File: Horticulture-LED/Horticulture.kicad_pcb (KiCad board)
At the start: 2 copper layers, 220 x 22 mm, 67 parts, among them J1 Conn_01x04_Male, J3 Conn_01x04_Male, J4 Conn_01x04_Male, SW1 SW-I2C, SW2 Rotary_Encoder_Switch, U1 TLE4309, U2 TLE4309, U3 TLE4309, U4 TLE4309, U6 STM32F030F4Px, U7 SSD1306

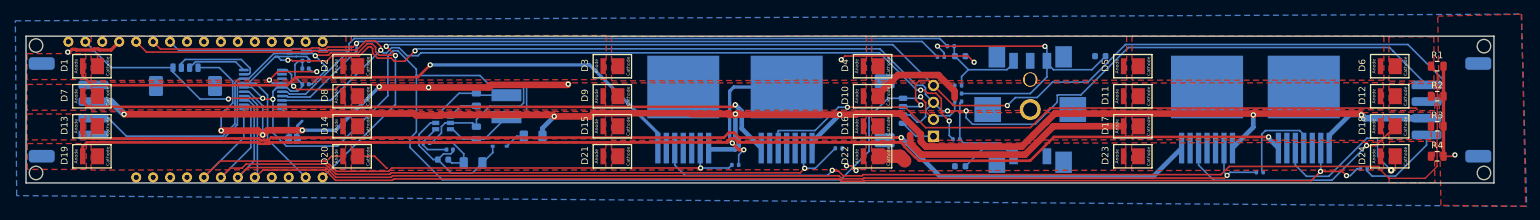
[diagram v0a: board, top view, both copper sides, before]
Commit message: More i2c connectors added, fp for 12c/pwm added, removed stm 32 fp, moved tle drivers
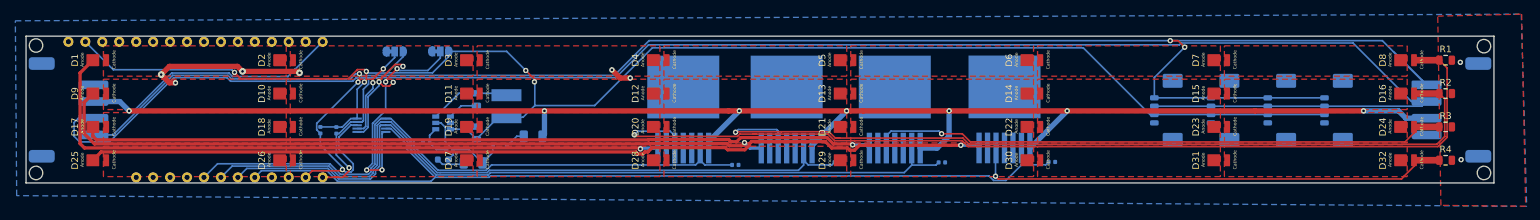
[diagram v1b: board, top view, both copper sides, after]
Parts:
- removed C3, C4, C5: 100nF, Capacitor_SMD:C_0603_1608Metric
- removed J1, Prgrm1: Conn_01x04_Male, Connector_Molex:Molex_PicoBlade_53398-0471_1x04-1MP_P1.25mm_Vertical
- removed R11, R12, R13, R14, R15, R16, R17: 10K2, Resistor_SMD:R_0402_1005Metric
- removed SW1: SW-I2C, Jumper:SolderJumper-2_P1.3mm_Open_RoundedPad1.0x1.5mm
- removed SW2: Rotary_Encoder_Switch, Rotary_Encoder:EC11J1524413-modiied
- removed U6: STM32F030F4Px, Package_SO:TSSOP-20_4.4x6.5mm_P0.65mm
- removed U7: SSD1306, Connector_PinHeader_2.54mm:PinHeader_1x04_P2.54mm_Vertical
- added 3.3v_i2c1: Conn_01x04_Male, Connector_Molex:Molex_PicoBlade_53398-0471_1x04-1MP_P1.25mm_Vertical, B.Cu at (210.3, 91.1)
- added 3.3v_i2c2: Conn_01x04_Male, Connector_Molex:Molex_PicoBlade_53398-0471_1x04-1MP_P1.25mm_Vertical, B.Cu at (218.8, 91.1)
- added 3.3v_i2c3: Conn_01x04_Male, Connector_Molex:Molex_PicoBlade_53398-0471_1x04-1MP_P1.25mm_Vertical, B.Cu at (235.8, 91.1)
- added 3.3v_i2c4: Conn_01x04_Male, Connector_Molex:Molex_PicoBlade_53398-0471_1x04-1MP_P1.25mm_Vertical, B.Cu at (227.3, 91.1)
- added D26: LED, LED_SMD:Sunplus-2835, F.Cu at (78.8, 98.6)
- added D27: LED, LED_SMD:Sunplus-2835, F.Cu at (106.8, 98.6)
- added D28: LED, LED_SMD:Sunplus-2835, F.Cu at (134.8, 98.6)
- added D29: LED, LED_SMD:Sunplus-2835, F.Cu at (162.8, 98.6)
- added D30: LED, LED_SMD:Sunplus-2835, F.Cu at (190.8, 98.6)
- added D31: LED, LED_SMD:Sunplus-2835, F.Cu at (218.8, 98.6)
- added D32: LED, LED_SMD:Sunplus-2835, F.Cu at (246.8, 98.6)
- added D33: D_Schottky, Diode_SMD:D_SOD-323, B.Cu at (111.0, 96.5)
- added JP1: i2c addr 1, Jumper:SolderJumper-3_P1.3mm_Bridged12_RoundedPad1.0x1.5mm_NumberLabels, B.Cu at (102.1, 82.3)
- added JP2: i2c addr 2, Jumper:SolderJumper-3_P1.3mm_Bridged12_RoundedPad1.0x1.5mm_NumberLabels, B.Cu at (95.2, 82.3)
- added U5: PCA9633DP2, Package_TO_SOT_SMD:SOT-552-1-nxp, B.Cu at (91.8, 93.3)
- D1, D10, D11, D12, D13, D14, D15, D16, D17, D18, D19, D2, D20, D21, D22, D23, D24, D3, D4, D5, D7, D8, D9: footprint LED_SMD:Sunplus-35 -> LED_SMD:Sunplus-2835
- D25: value D_Schottky -> LED; footprint Diode_SMD:D_SOD-323 -> LED_SMD:Sunplus-2835; moved to F.Cu
- D6: value LED-purple -> LED; footprint LED_SMD:Sunplus-35 -> LED_SMD:Sunplus-2835
- moved D7 170.3 mm to (218.8, 83.6), turned to 0 degrees
- moved D18 164.3 mm to (78.8, 93.6), turned to 0 degrees
- moved D8 159.3 mm to (246.8, 83.6), turned to 0 degrees
- moved D17 153.8 mm to (50.8, 93.6), turned to 0 degrees
- moved D13 114.4 mm to (162.8, 88.6), turned to 0 degrees
- moved D12 108.3 mm to (134.8, 88.6), turned to 0 degrees
- moved D14 103.4 mm to (190.8, 88.6), turned to 0 degrees
- moved D11 97.8 mm to (106.8, 88.6), turned to 0 degrees
- moved D15 92.4 mm to (218.8, 88.6), turned to 0 degrees
- moved D10 86.8 mm to (78.8, 88.6), turned to 0 degrees
- moved D16 81.4 mm to (246.8, 88.6), turned to 0 degrees
- moved D9 75.8 mm to (50.8, 88.6), turned to 0 degrees
- moved D25 60.3 mm to (50.8, 98.6)
- moved D19 58.4 mm to (106.8, 93.6), turned to 0 degrees
- moved D6 52.3 mm to (190.8, 83.6), turned to 0 degrees
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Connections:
- A1 pad A0: Enc-bt1 -> Net-(A1-PadA0)
- A1 pad A1: Enc-B -> Net-(A1-PadA1)
- A1 pad A2: Enc-A -> Net-(A1-PadA2)
- D13 pad 2: Net-(D13-Pad2) -> Net-(D12-Pad1)
- D17 pad 2: Net-(D16-Pad1) -> Net-(D17-Pad2)
- D19 pad 2: Net-(D19-Pad2) -> Net-(D18-Pad1)
- D25 pad 1: Net-(Cin1-Pad1) -> Net-(D25-Pad1)
- D7 pad 2: Net-(D7-Pad2) -> Net-(D6-Pad1)
- D9 pad 2: Net-(D8-Pad1) -> Net-(D9-Pad2)
- F1 pad 1: Net-(D25-Pad2) -> Net-(D33-Pad2)
- F1 pad 2: VDC -> +24vdc
- J3 pad 3: VDC -> +24vdc
- J4 pad 3: VDC -> +24vdc
- R1 pad 1: Net-(D6-Pad1) -> Net-(D8-Pad1)
- R2 pad 1: Net-(D12-Pad1) -> Net-(D16-Pad1)
- R3 pad 1: Net-(D18-Pad1) -> Net-(D24-Pad1)
- R4 pad 1: Net-(D24-Pad1) -> Net-(D32-Pad1)
- U1 pad 1: VDC -> +24vdc
- U1 pad 5: Net-(D6-Pad1) -> Net-(D8-Pad1)
- U2 pad 1: VDC -> +24vdc
- U2 pad 5: Net-(D12-Pad1) -> Net-(D16-Pad1)
- U2 pad 7: Net-(D7-Pad2) -> Net-(D9-Pad2)
- U3 pad 1: VDC -> +24vdc
- U3 pad 5: Net-(D18-Pad1) -> Net-(D24-Pad1)
- U3 pad 7: Net-(D13-Pad2) -> Net-(D17-Pad2)
- U4 pad 1: VDC -> +24vdc
- U4 pad 5: Net-(D24-Pad1) -> Net-(D32-Pad1)
- U4 pad 7: Net-(D19-Pad2) -> Net-(D25-Pad2)
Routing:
- net Net-(D19-Pad2): track 279.6 -> 0.00 mm, vias 1 -> 0
- net +24vdc: track 0.00 -> 272.4 mm, vias 0 -> 7
- net VDC: track 243.8 -> 0.00 mm, vias 6 -> 0
- net GND: track 256.0 -> 49.6 mm, vias 15 -> 11
- net Net-(D13-Pad2): track 171.6 -> 0.00 mm, vias 1 -> 0
- net Enc-bt1: track 151.8 -> 0.00 mm, vias 3 -> 0
- net Net-(D8-Pad1): track 0.00 -> 148.6 mm, vias 0 -> 1
- net Enc-B: track 136.4 -> 0.00 mm, vias 1 -> 0
- net Net-(D6-Pad1): track 135.7 -> 0.00 mm, vias 1 -> 0
- net Net-(D25-Pad2): track 3.17 -> 135.6 mm, vias 0 -> 1
- net Enc-A: track 132.0 -> 0.00 mm
- net Net-(D17-Pad2): track 0.00 -> 119.1 mm, vias 0 -> 1
- net Net-(D9-Pad2): track 0.00 -> 109.4 mm, vias 0 -> 1
- net Net-(D7-Pad2): track 107.7 -> 0.00 mm, vias 1 -> 0
- net Net-(D12-Pad1): track 102.4 -> 0.00 mm, vias 1 -> 0
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- added copper zone on F.Cu, net Net-(D25-Pad1)
- added copper zone on F.Cu, net Net-(D26-Pad1)
- added copper zone on F.Cu, net Net-(D27-Pad1)
- added copper zone on F.Cu, net Net-(D28-Pad1)
- added copper zone on F.Cu, net Net-(D29-Pad1)
- added copper zone on F.Cu, net Net-(D30-Pad1)
- added copper zone on F.Cu, net Net-(D31-Pad1)
- removed copper zone on F.Cu, net Net-(D1-Pad2)
- removed copper zone on F.Cu, net Net-(D13-Pad2)
- removed copper zone on F.Cu, net Net-(D16-Pad1)
- removed copper zone on F.Cu, net Net-(D19-Pad2)
- removed copper zone on F.Cu, net Net-(D24-Pad1)
- removed copper zone on F.Cu, net Net-(D7-Pad2)
- removed copper zone on F.Cu, net Net-(D8-Pad1)
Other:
- net class Led-Driver: clearance 0.2 -> 0.1; trace_width 0.25 -> 0.8
- net class Led-power: clearance 0.2 -> 0.1; trace_width 0.25 -> 1
- net class VDC: clearance 0.2 -> 0.1; trace_width 1 -> 0.8; via_dia 0.8 -> 1
- net class ymse power: trace_width 0.4 -> 0.5
- board text added: "1.SCL"
- board text added: "2.SDA"
- board text added: "3.+24v"
- board text added: "4.GND"
- board text added: "Horticulture-rev-3.4.0"
- board text removed: "Horticulture-rev-3.3.1"

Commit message: ryddet i resistorer
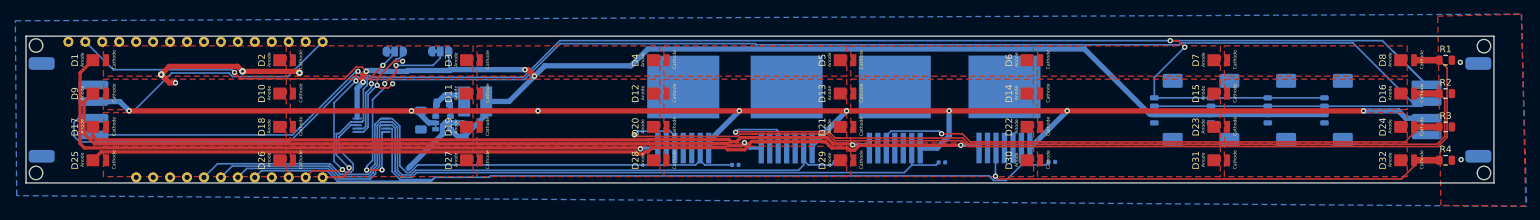
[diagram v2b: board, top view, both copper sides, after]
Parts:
- removed Cinx1: 100nF, Capacitor_SMD:C_0603_1608Metric
- removed D33: D_Schottky, Diode_SMD:D_SOD-323
- removed F1: Polyfuse, Fuse:Fuse_1206_3216Metric
- removed R5, R6: 4.7K, Resistor_SMD:R_0402_1005Metric
- removed Renb1, Rent1: 10k, Resistor_SMD:R_0402_1005Metric
- moved Cin1 10.1 mm to (99.2, 92.6), turned to 270 degrees
- moved Cboot1 5.04 mm to (102.5, 90.0), turned to 0 degrees
- moved L1 4.74 mm to (107.3, 89.8), turned to 270 degrees
- moved Cout1 1.88 mm to (105.7, 94.1)
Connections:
- A1 pad A0: Net-(A1-PadA0) -> (no net)
- A1 pad A1: Net-(A1-PadA1) -> (no net)
- A1 pad A2: Net-(A1-PadA2) -> (no net)
- A1 pad A3: Net-(A1-PadA3) -> (no net)
- A1 pad A4: Net-(A1-PadA4) -> (no net)
- A1 pad A5: Net-(A1-PadA5) -> (no net)
- A1 pad D2: Net-(A1-PadD2) -> (no net)
- A1 pad D3: Net-(A1-PadD3) -> (no net)
- A1 pad D8: Net-(A1-PadD8) -> (no net)
- A1 pad EN: Net-(A1-PadEN) -> (no net)
- A1 pad LI+: Net-(A1-PadLI+) -> (no net)
- A1 pad MD: Net-(A1-PadMD) -> (no net)
- A1 pad MI: Net-(A1-PadMI) -> (no net)
- A1 pad MO: Net-(A1-PadMO) -> (no net)
- A1 pad RESET: Net-(A1-PadRESET) -> (no net)
- A1 pad RX: Net-(A1-PadRX) -> (no net)
- A1 pad SCK: Net-(A1-PadSCK) -> (no net)
- A1 pad TX: Net-(A1-PadTX) -> (no net)
- A1 pad VUSB: Net-(A1-PadVUSB) -> (no net)
- Cin1 pad 1: Net-(Cin1-Pad1) -> +24vdc
- VR1 pad 4: Net-(Renb1-Pad1) -> +24vdc
- VR1 pad 5: Net-(Cin1-Pad1) -> +24vdc
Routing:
- net Net-(Cin1-Pad1): track 15.7 -> 0.00 mm
- net +3.3V: track 238.5 -> 253.8 mm
- net Net-(Renb1-Pad1): track 5.37 -> 0.00 mm
- net Net-(Cboot1-Pad1): track 12.2 -> 7.07 mm
- net GND: track 49.6 -> 54.5 mm, vias 11 -> 9
- net UC-pwm4: track 135.2 -> 138.8 mm
- net UC-pwm3: track 120.2 -> 123.9 mm
- net UC-pwm2: track 109.4 -> 113.0 mm
- net UC-pwm1: track 94.3 -> 97.6 mm
- net Net-(D33-Pad2): track 3.17 -> 0.00 mm
- net +24vdc: track 272.4 -> 275.1 mm, vias 7 -> 8
- net Net-(Cboot1-Pad2): track 4.57 -> 2.08 mm
- net I2c-SCL: track 289.5 -> 287.6 mm

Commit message: fixed GND copper with
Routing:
- net GND: track 54.5 -> 70.0 mm
- net (no net): track 0.00 -> 3.49 mm, vias 0 -> 2
- net Net-(JP1-Pad2): track 34.0 -> 36.1 mm

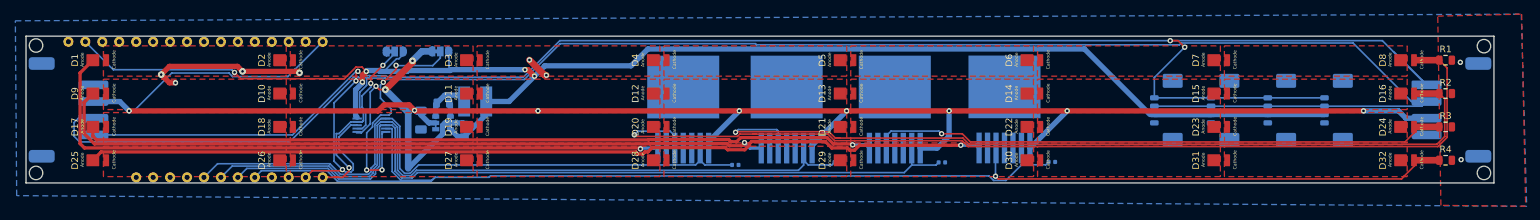
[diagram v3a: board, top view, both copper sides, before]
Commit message: Satt Farge på LED
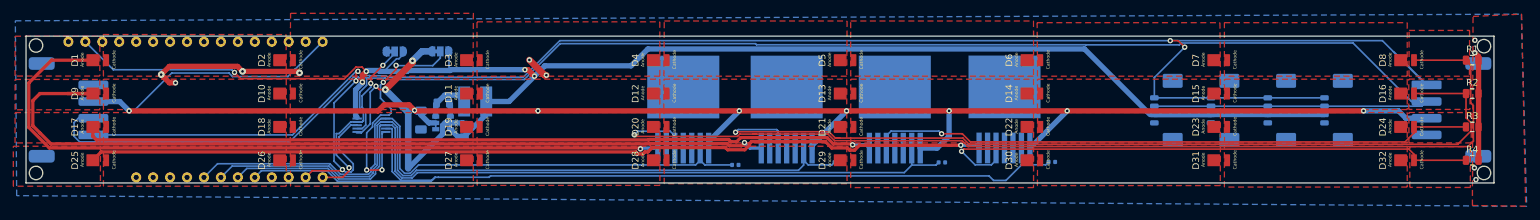
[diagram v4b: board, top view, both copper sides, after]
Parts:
- moved R1 4.00 mm to (256.8, 83.6)
- moved R2 4.00 mm to (256.8, 88.6)
- moved R3 4.00 mm to (256.8, 93.6)
- moved R4 4.00 mm to (256.8, 98.6)
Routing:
- net Net-(D9-Pad2): track 109.4 -> 128.0 mm
- net GND: track 70.0 -> 86.3 mm, vias 9 -> 11
- net Net-(D1-Pad2): track 100.3 -> 113.3 mm
- net Net-(D32-Pad1): track 72.5 -> 85.1 mm
- net Net-(D8-Pad1): track 148.6 -> 157.0 mm
- net Net-(D16-Pad1): track 127.5 -> 135.1 mm
- net Net-(D24-Pad1): track 87.0 -> 91.0 mm
- added copper zone on F.Cu, net Net-(D1-Pad2)
- added copper zone on F.Cu, net Net-(D16-Pad1)
- added copper zone on F.Cu, net Net-(D17-Pad2)
- added copper zone on F.Cu, net Net-(D24-Pad1)
- added copper zone on F.Cu, net Net-(D25-Pad2)
- added copper zone on F.Cu, net Net-(D32-Pad1)
- added copper zone on F.Cu, net Net-(D8-Pad1)
- added copper zone on F.Cu, net Net-(D9-Pad2)

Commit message: Enda mer kobber
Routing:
- net GND: track 86.3 -> 133.1 mm
- net I2c-SCL: track 287.6 -> 244.7 mm, vias 5 -> 3
- net I2c-SDA: track 283.0 -> 267.7 mm
- net +3.3V: track 254.0 -> 239.9 mm
